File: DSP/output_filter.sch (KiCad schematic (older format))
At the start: 5 parts

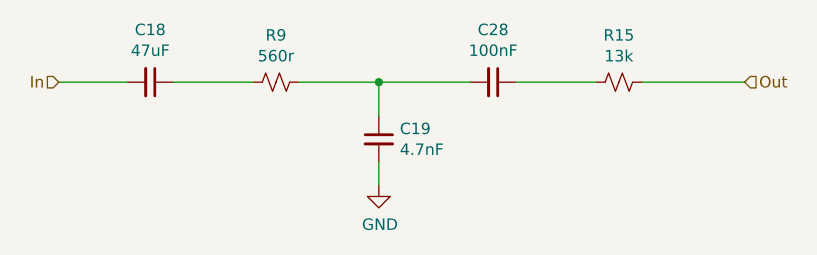
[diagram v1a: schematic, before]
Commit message: finished DSP and AMP
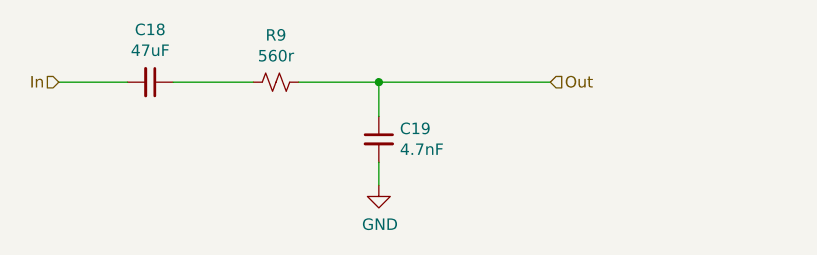
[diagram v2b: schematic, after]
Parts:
- removed C11: 100nF, Capacitor_SMD:C_0805_2012Metric_Pad1.15x1.40mm_HandSolder, symbol Device:C_Small
- removed R12: 13k, Resistor_SMD:R_0805_2012Metric_Pad1.15x1.40mm_HandSolder, symbol Device:R_Small_US
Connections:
- net Out: now also C13.1, R6.1
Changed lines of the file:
@@
 $Descr A4 11693 8268
 encoding utf-8
-Sheet 2 5
+Sheet 5 5
 Title ""
 Date ""
@@
 Text HLabel 3800 4000 0    50   Input ~ 0
 In
-Text HLabel 6800 4000 2    50   Input ~ 0
+Text HLabel 5950 4000 2    50   Input ~ 0
 Out
 $Comp
@@
 	1    0    0    -1
 $EndComp
-$Comp
-L Device:C_Small C11
-U 1 1 5DEF160F
-P 5700 4000
-AR Path="/5DE47C86/5DEF160F" Ref="C11"  Part="1"
-AR Path="/5DE4A02D/5DEF160F" Ref="C26"  Part="1"
-AR Path="/5DE4AB46/5DEF160F" Ref="C27"  Part="1"
-AR Path="/5DE4B545/5DEF160F" Ref="C28"  Part="1"
-F 0 "C28" V 5471 4000 50  0000 C CNN
-F 1 "100nF" V 5562 4000 50  0000 C CNN
-F 2 "Capacitor_SMD:C_0805_2012Metric_Pad1.15x1.40mm_HandSolder" H 5700 4000 50  0001 C CNN
-F 3 "~" H 5700 4000 50  0001 C CNN
-	1    5700 4000
-	0    1    1    0
-$EndComp
-$Comp
-L Device:R_Small_US R12
-U 1 1 5DEF1615
-P 6250 4000
-AR Path="/5DE47C86/5DEF1615" Ref="R12"  Part="1"
-AR Path="/5DE4A02D/5DEF1615" Ref="R13"  Part="1"
-AR Path="/5DE4AB46/5DEF1615" Ref="R14"  Part="1"
-AR Path="/5DE4B545/5DEF1615" Ref="R15"  Part="1"
-F 0 "R15" V 6045 4000 50  0000 C CNN
-F 1 "13k" V 6136 4000 50  0000 C CNN
-F 2 "Resistor_SMD:R_0805_2012Metric_Pad1.15x1.40mm_HandSolder" H 6250 4000 50  0001 C CNN
-F 3 "~" H 6250 4000 50  0001 C CNN
-	1    6250 4000
-	0    1    1    0
-$EndComp
 Wire Wire Line
-	5800 4000 6150 4000
-Wire Wire Line
-	5200 4000 5600 4000
+	5200 4000 5950 4000
 Connection ~ 5200 4000
-Wire Wire Line
-	6350 4000 6800 4000
 $EndSCHEMATC
